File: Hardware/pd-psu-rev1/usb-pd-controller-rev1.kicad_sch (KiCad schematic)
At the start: 18 parts, among them CN3 KF301-2P, J2 USB_C_Receptacle_USB2.0_16P, SW1 RotaryEncoder_Switch, U1 INA219AxD, U2 CH224K, U3 CH32V003FxPx, U4 78L33

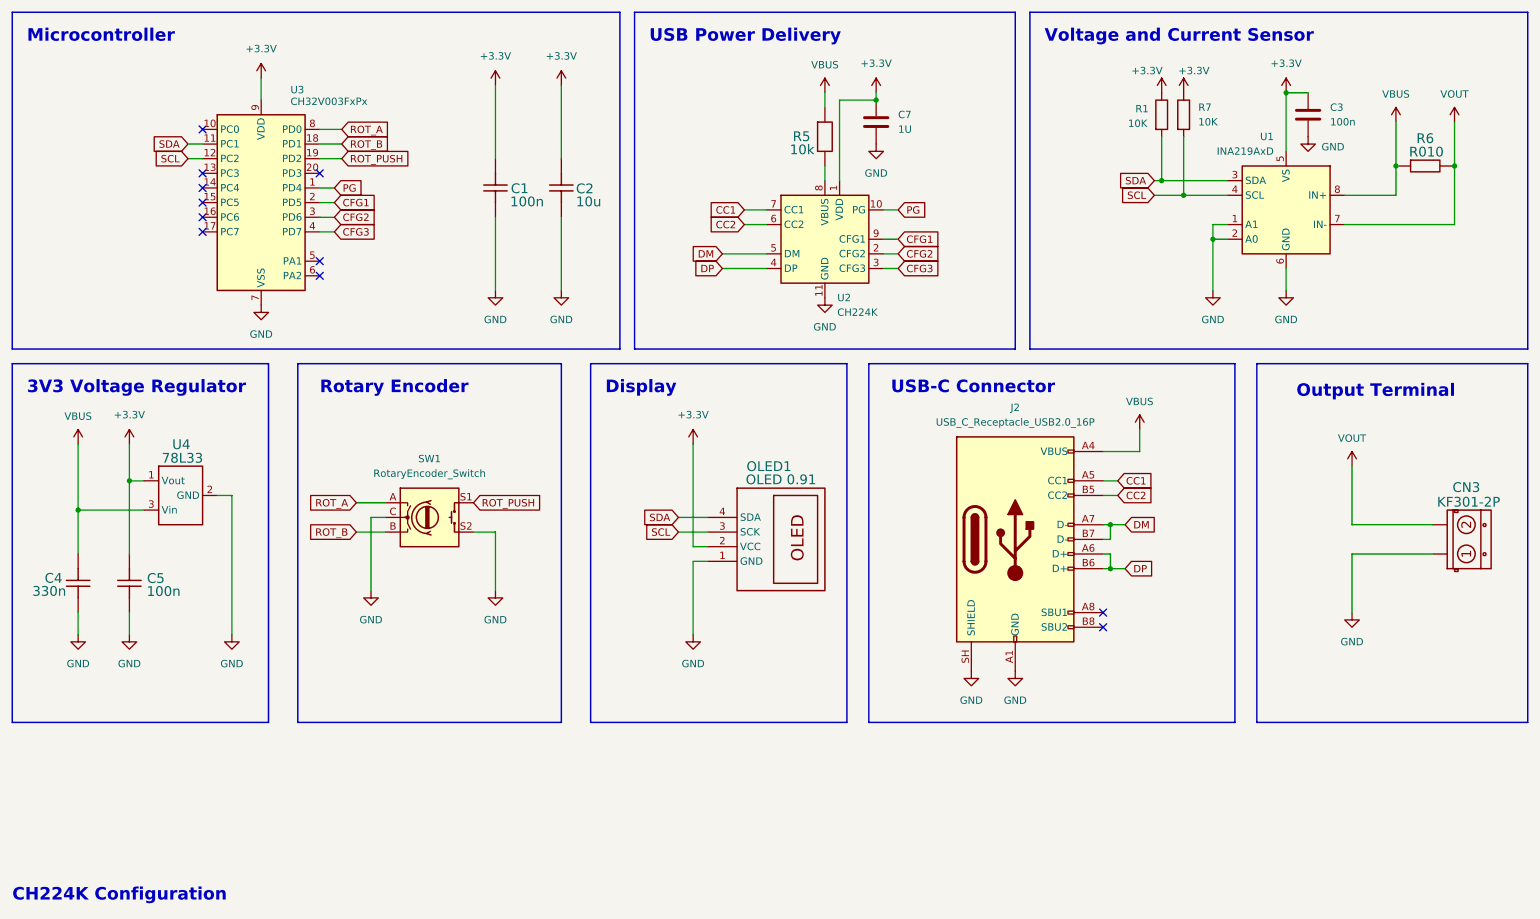
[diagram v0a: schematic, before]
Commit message: update pcb + add some 3d files
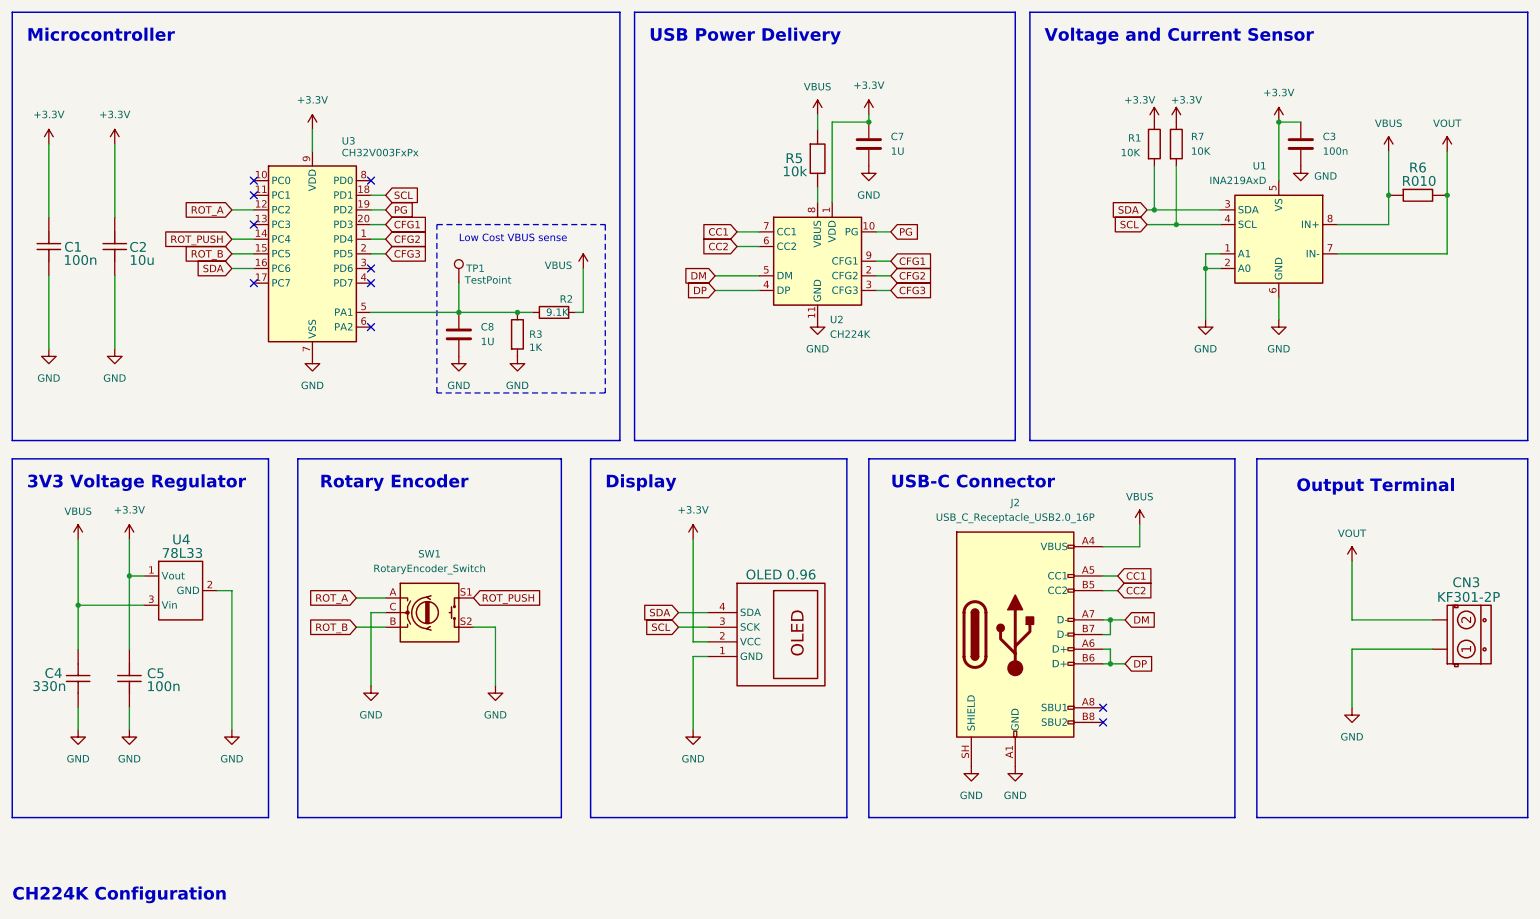
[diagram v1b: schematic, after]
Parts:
- added C8: 1U, Capacitor_SMD:C_0805_2012Metric, symbol Device:C
- added R2: 9.1K, Resistor_SMD:R_0805_2012Metric, symbol Device:R
- added R3: 1K, Resistor_SMD:R_0805_2012Metric, symbol Device:R
- added TP1: TestPoint, TestPoint:TestPoint_Pad_D1.5mm, symbol Connector:TestPoint
- C1, C3, C4, C5, C7: footprint (none) -> Capacitor_SMD:C_0805_2012Metric
- C2: footprint (none) -> Capacitor_SMD:C_1206_3216Metric
- CN3: footprint (none) -> Connector_Wire:SolderWire-6sqmm_1x02_P14mm_D3.5mm_OD7mm
- J2: footprint (none) -> Connector_USB:USB_C_Receptacle_GCT_USB4105-xx-A_16P_TopMnt_Horizontal
- OLED1: value OLED 0.91 -> OLED 0.96; footprint (none) -> Connector_PinSocket_2.54mm:PinSocket_1x04_P2.54mm_Vertical
- R1, R5, R6, R7: footprint (none) -> Resistor_SMD:R_0805_2012Metric
- SW1: footprint (none) -> Rotary_Encoder:RotaryEncoder_Alps_EC11E_Vertical_H20mm
- U4: footprint (none) -> Package_TO_SOT_SMD:SOT-89-3
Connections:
- net CFG1: now also U3.20 (PD3); no longer U3.2 (PD5)
- net CFG2: now also U3.1 (PD4); no longer U3.3 (PD6)
- net CFG3: now also U3.2 (PD5); no longer U3.4 (PD7)
- net GND: now also C8.2, R3.2
- net PG: now also U3.19 (PD2); no longer U3.1 (PD4)
- net ROT_A: now also U3.12 (PC2); no longer U3.8 (PD0)
- net ROT_B: now also U3.15 (PC5); no longer U3.18 (PD1)
- net ROT_PUSH: now also U3.14 (PC4); no longer U3.19 (PD2)
- net SCL: now also U3.18 (PD1); no longer U3.12 (PC2)
- net SDA: now also U3.16 (PC6); no longer U3.11 (PC1)
- net VBUS: now also R2.2
- net at U3.5 (PA1): now also C8.1, R2.1, R3.1, TP1.1
- no-connect marks 11 -> 10
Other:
- note added: "Low Cost VBUS sense"
- moved on the sheet: C1, C2, C3, C4, C5, C7, CN3, J2, R1, R5, R6, R7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

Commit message: update schematic
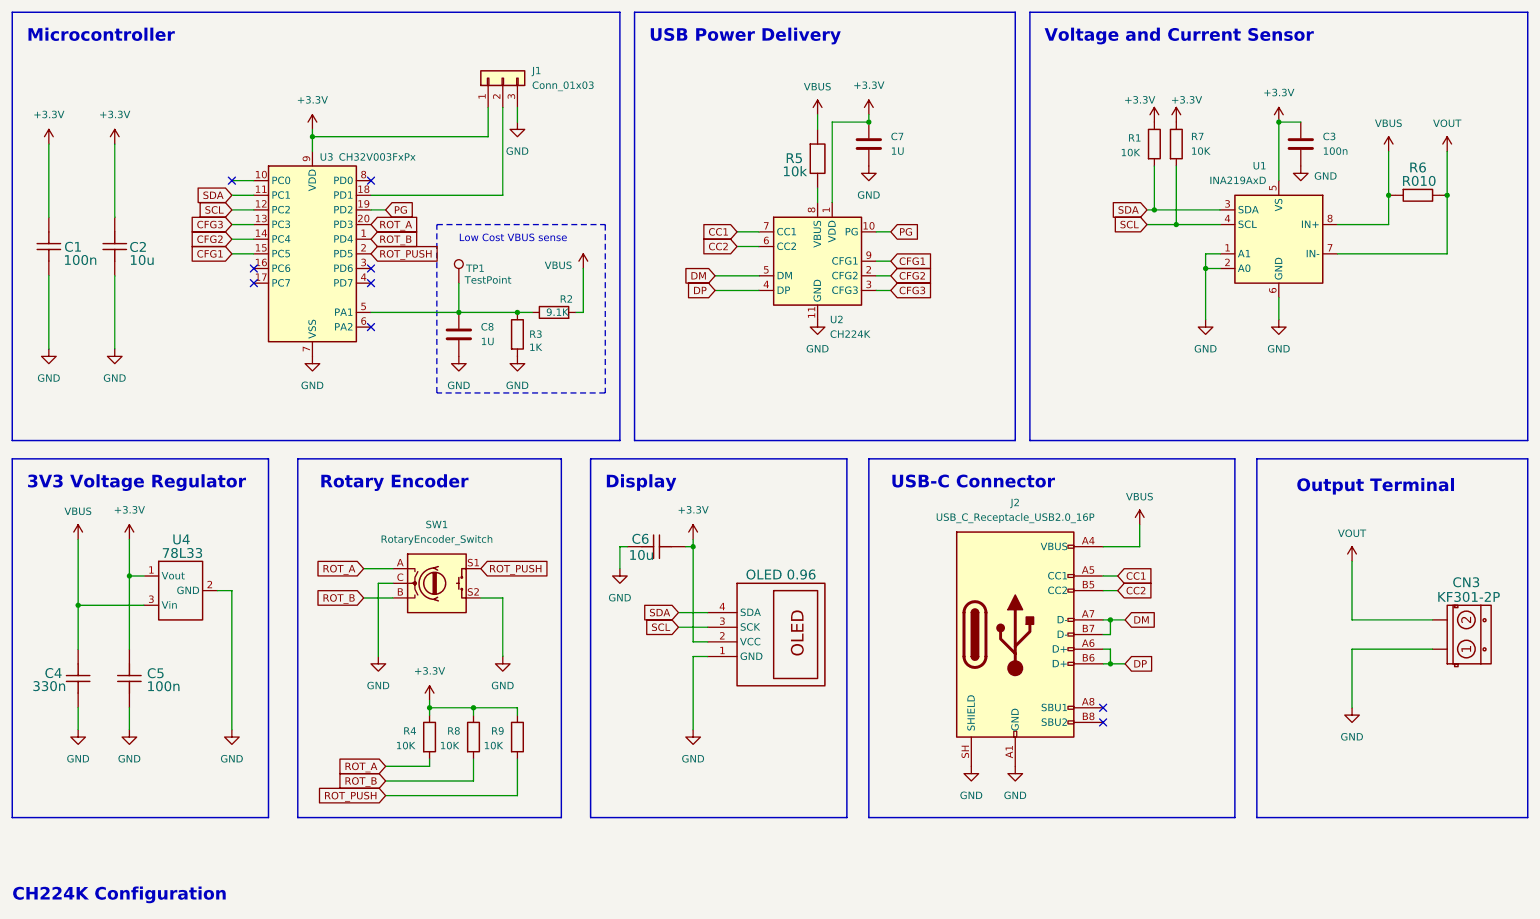
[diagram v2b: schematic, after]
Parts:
- added C6: 10u, Capacitor_SMD:C_1206_3216Metric, symbol CL10A106MA8NRNC
- added J1: Conn_01x03, Connector_PinHeader_2.54mm:PinHeader_1x03_P2.54mm_Vertical, symbol Connector_Generic:Conn_01x03
- added R4, R8, R9: 10K, Resistor_SMD:R_0805_2012Metric, symbol Device:R
- R6: footprint Resistor_SMD:R_0805_2012Metric -> Resistor_SMD:R_2512_6332Metric
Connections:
- net +3.3V: now also C6.2, J1.1 (Pin_1), R4.1, R8.1, R9.1
- net CFG1: now also U3.15 (PC5); no longer U3.20 (PD3)
- net CFG2: now also U3.14 (PC4); no longer U3.1 (PD4)
- net CFG3: now also U3.13 (PC3); no longer U3.2 (PD5)
- net GND: now also C6.1, J1.3 (Pin_3)
- net ROT_A: now also U3.20 (PD3), R4.2; no longer U3.12 (PC2)
- net ROT_B: now also U3.1 (PD4), R8.2; no longer U3.15 (PC5)
- net ROT_PUSH: now also U3.2 (PD5), R9.2; no longer U3.14 (PC4)
- net SCL: now also U3.12 (PC2); no longer U3.18 (PD1)
- net SDA: now also U3.11 (PC1); no longer U3.16 (PC6)
- new net: J1.2 (Pin_2), U3.18 (PD1)
- no-connect marks 10 -> 9
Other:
- moved on the sheet: SW1
